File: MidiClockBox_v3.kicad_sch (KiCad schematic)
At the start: 69 parts, among them J1 Midi In 0, J10 Display, J11 Midi Out 3, J12 Midi Out 4, J13 Midi Out 5, J14 Sync Out 0, J15 Sync Out 1, J16 Conn_01x08, J2 ICSP, J3 Conn_02x09_Odd_Even, J4 Conn_02x04_Odd_Even, J5 Conn_02x12_Counter_Clockwise, J6 Midi Out 0, J7 Midi Out 1, J8 Midi Out 2, J9 WS2812, SW1 RotaryEncoder_Switch, U1 CD74HC4067SM, U2 74LS241, U3 6N138, U4 74HC595, U6 74LS08, U7 74LS08, U8 74HC595, U9 74LS241

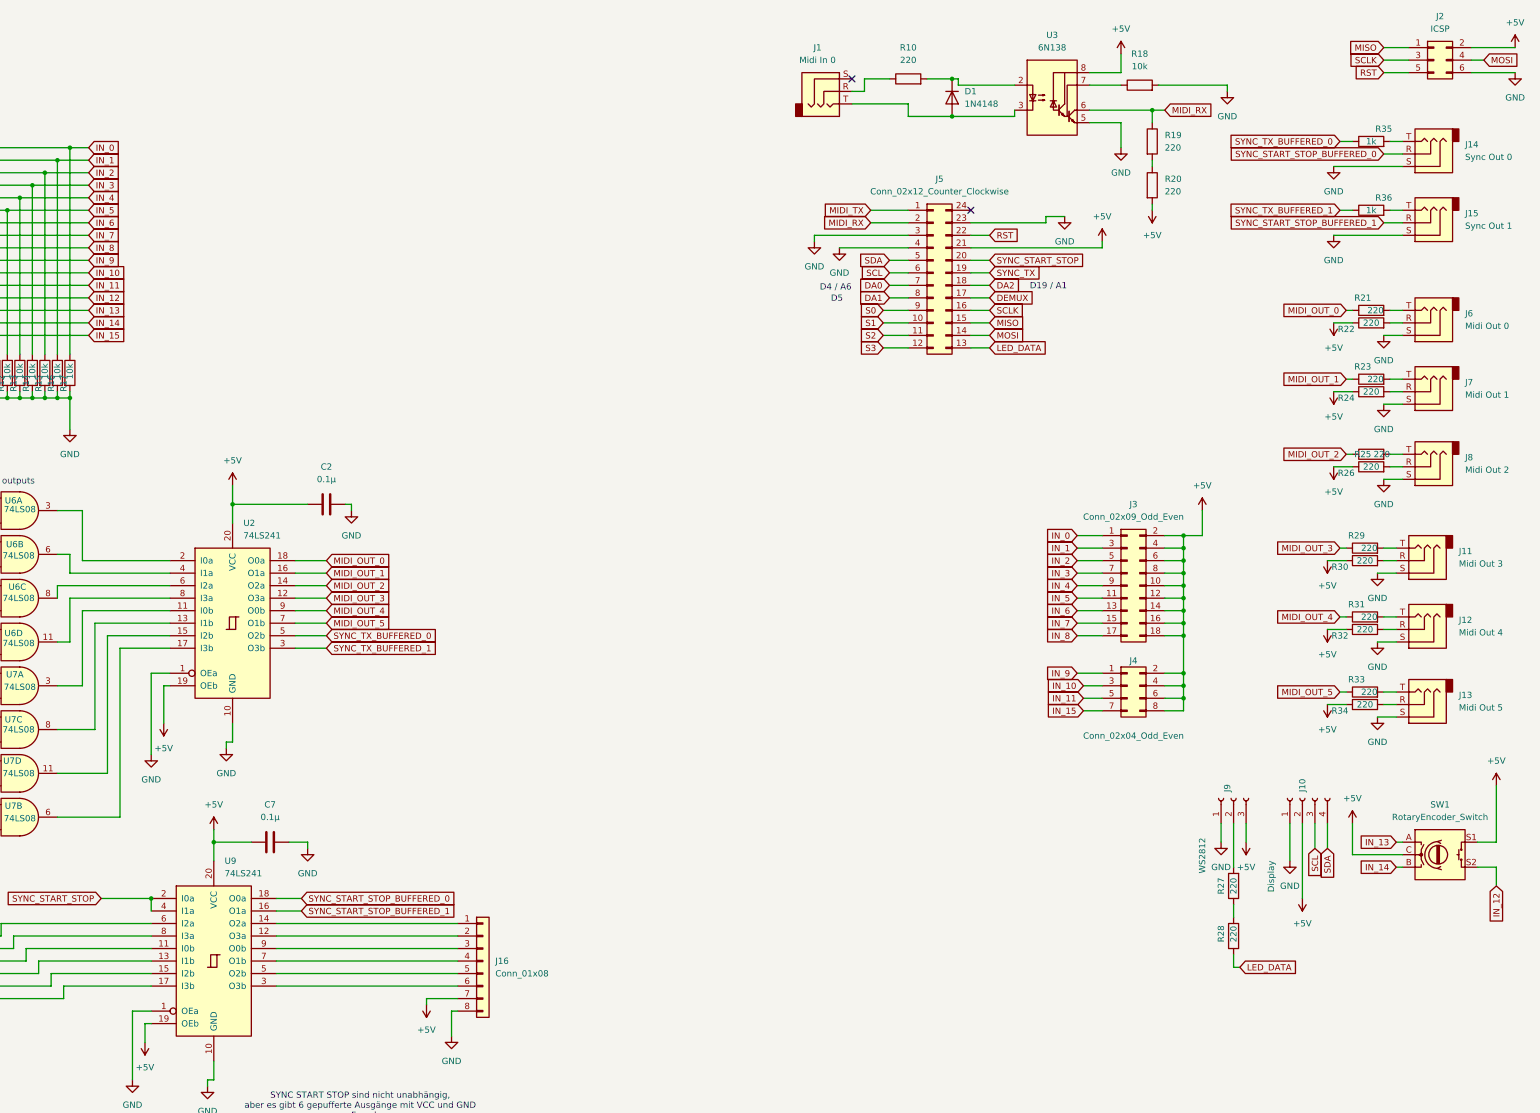
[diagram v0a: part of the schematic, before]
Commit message: add edge cuts
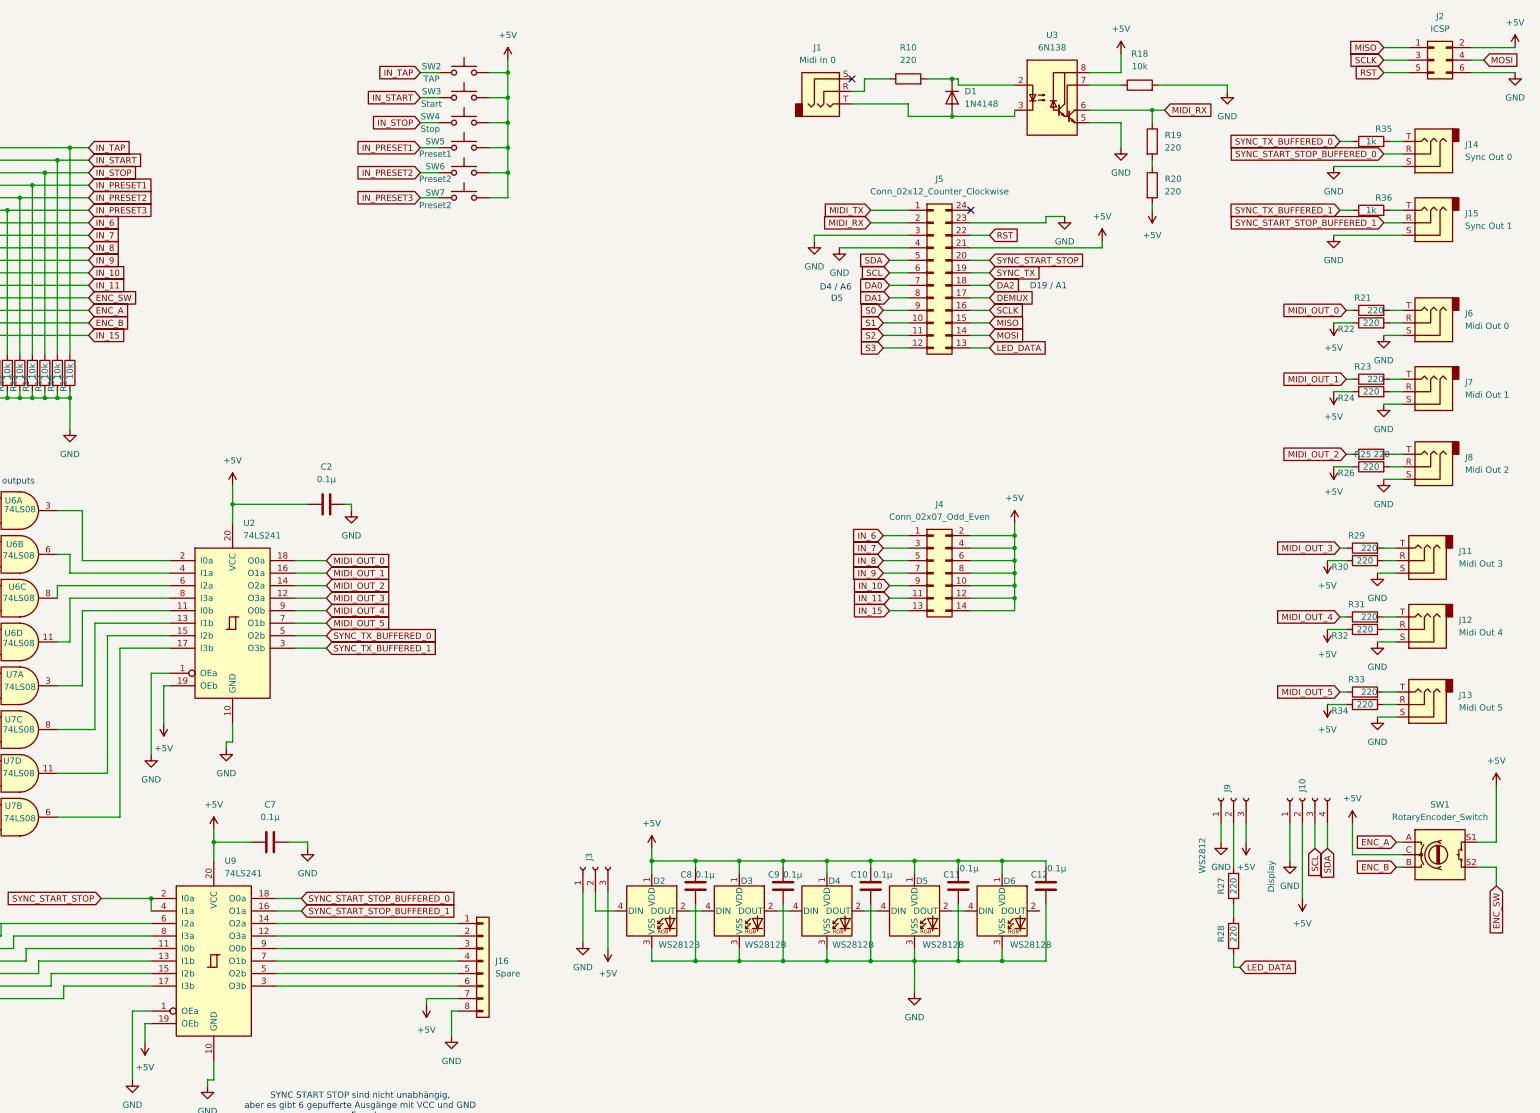
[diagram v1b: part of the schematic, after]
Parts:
- removed J3: Conn_02x09_Odd_Even, Connector_PinHeader_2.54mm:PinHeader_2x09_P2.54mm_Vertical, symbol Connector_Generic:Conn_02x09_Odd_Even
- removed J4: Conn_02x04_Odd_Even, Connector_PinHeader_2.54mm:PinHeader_2x04_P2.54mm_Vertical, symbol Connector_Generic:Conn_02x04_Odd_Even
- added C10, C11, C12, C8, C9: 0.1µ, Capacitor_SMD:C_0603_1608Metric, symbol Device:C
- added D2, D3, D4, D5, D6: WS2812B, LED_SMD:LED_WS2812B_PLCC4_5.0x5.0mm_P3.2mm, symbol LED:WS2812B
- added J3: WS2812, Connector_PinHeader_2.54mm:PinHeader_1x03_P2.54mm_Vertical, symbol Connector:Conn_01x03_Socket
- added J4: Conn_02x07_Odd_Even, Connector_PinHeader_2.54mm:PinHeader_2x07_P2.54mm_Vertical, symbol Connector_Generic:Conn_02x07_Odd_Even
- added SW2: TAP, Button_Switch_THT:SW_PUSH-12mm_Wuerth-430476085716, symbol Switch:SW_Push
- added SW3: Start, Button_Switch_THT:SW_PUSH-12mm_Wuerth-430476085716, symbol Switch:SW_Push
- added SW4: Stop, Button_Switch_THT:SW_PUSH-12mm_Wuerth-430476085716, symbol Switch:SW_Push
- added SW5: Preset1, Button_Switch_THT:SW_PUSH-12mm_Wuerth-430476085716, symbol Switch:SW_Push
- added SW6, SW7: Preset2, Button_Switch_THT:SW_PUSH-12mm_Wuerth-430476085716, symbol Switch:SW_Push
- J16: value Conn_01x08 -> Spare
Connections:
- net +5V: now also C10.1, C11.1, C12.1, C8.1, C9.1, D2.1 (VDD), D3.1 (VDD), D4.1 (VDD), D5.1 (VDD), D6.1 (VDD), J3.3 (Pin_3), J4.10 (Pin_10), J4.12 (Pin_12), J4.14 (Pin_14), J4.2 (Pin_2), J4.4 (Pin_4), J4.6 (Pin_6), J4.8 (Pin_8), SW2.2, SW3.2, SW4.2, SW5.2, SW6.2, SW7.2
- net GND: now also C10.2, C11.2, C12.2, C8.2, C9.2, D2.3 (VSS), D3.3 (VSS), D4.3 (VSS), D5.3 (VSS), D6.3 (VSS), J3.1 (Pin_1)
- net IN_10: now also J4.9 (Pin_9)
- net IN_11: now also J4.11 (Pin_11)
- net IN_15: now also J4.13 (Pin_13)
- net IN_6: now also J4.1 (Pin_1)
- net IN_7: now also J4.3 (Pin_3)
- net IN_8: now also J4.5 (Pin_5)
- net IN_9: now also J4.7 (Pin_7)
- net IN_0 renamed IN_TAP
- net IN_TAP: now also SW2.1
- net IN_1 renamed IN_START
- net IN_START: now also SW3.1
- net IN_12 renamed ENC_SW
- net IN_13 renamed ENC_A
- net IN_14 renamed ENC_B
- net IN_2 renamed IN_STOP
- net IN_STOP: now also SW4.1
- net IN_3 renamed IN_PRESET1
- net IN_PRESET1: now also SW5.1
- net IN_4 renamed IN_PRESET2
- net IN_PRESET2: now also SW6.1
- net IN_5 renamed IN_PRESET3
- net IN_PRESET3: now also SW7.1
- new net: D2.2 (DOUT), D3.4 (DIN)
- new net: D2.4 (DIN), J3.2 (Pin_2)
- new net: D4.2 (DOUT), D5.4 (DIN)
- new net: D3.2 (DOUT), D4.4 (DIN)
- new net: D5.2 (DOUT), D6.4 (DIN)

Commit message: add recent changes
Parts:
- SW7: value Preset2 -> Preset3
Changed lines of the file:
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@@
 			)
 		)
-		(property "Value" "Preset2"
+		(property "Value" "Preset3"
 			(at 183.388 52.324 0)
 			(effects

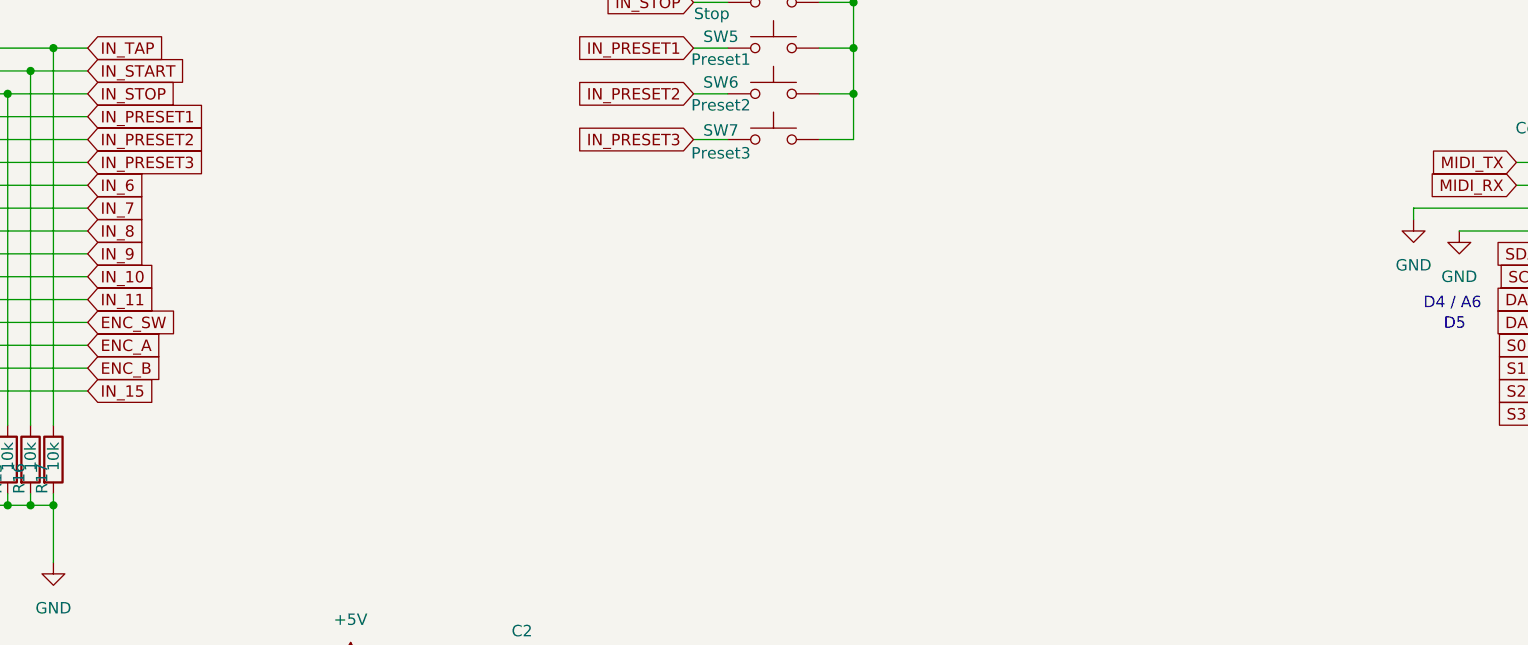
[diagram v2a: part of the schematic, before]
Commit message: add breakout connectors for sync-out and midi-in
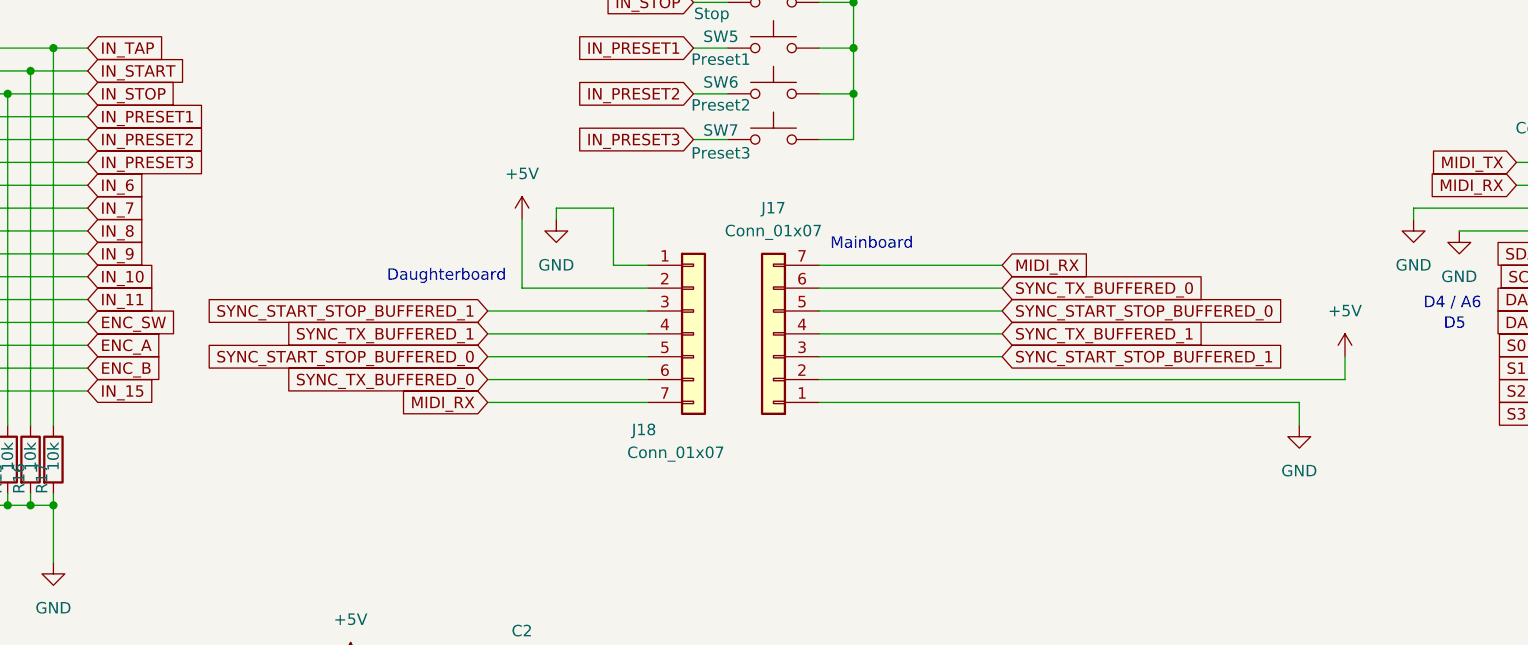
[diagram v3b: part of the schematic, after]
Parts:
- added J17, J18: Conn_01x07, Connector_PinHeader_2.54mm:PinHeader_1x07_P2.54mm_Vertical, symbol Connector_Generic:Conn_01x07
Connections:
- net +5V: now also J17.2 (Pin_2), J18.2 (Pin_2)
- net GND: now also J17.1 (Pin_1), J18.1 (Pin_1)
- net MIDI_RX: now also J17.7 (Pin_7), J18.7 (Pin_7)
- net SYNC_START_STOP_BUFFERED_0: now also J17.5 (Pin_5), J18.5 (Pin_5)
- net SYNC_START_STOP_BUFFERED_1: now also J17.3 (Pin_3), J18.3 (Pin_3)
- net SYNC_TX_BUFFERED_0: now also J17.6 (Pin_6), J18.6 (Pin_6)
- net SYNC_TX_BUFFERED_1: now also J17.4 (Pin_4), J18.4 (Pin_4)
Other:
- note added: "Daughterboard"
- note added: "Mainboard"

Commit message: pcb looks complete
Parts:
- added J19, J20: Conn_02x05_Odd_Even, Connector_PinHeader_2.54mm:PinHeader_2x05_P2.54mm_Vertical, symbol Connector_Generic:Conn_02x05_Odd_Even
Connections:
- net +5V: now also J19.2 (Pin_2), J20.2 (Pin_2)
- net DEMUX: now also J19.3 (Pin_3), J20.3 (Pin_3)
- net GND: now also J19.1 (Pin_1), J20.1 (Pin_1)
- net LED_DATA: now also D2.4 (DIN), J3.2 (Pin_2), J9.2 (Pin_2), J19.10 (Pin_10), J20.10 (Pin_10); no longer J5.13 (Pin_13)
- net S0: now also J19.4 (Pin_4), J20.4 (Pin_4)
- net S1: now also J19.5 (Pin_5), J20.5 (Pin_5)
- net S2: now also J19.6 (Pin_6), J20.6 (Pin_6)
- net S3: now also J19.7 (Pin_7), J20.7 (Pin_7)
- net SCL: now also J19.9 (Pin_9), J20.9 (Pin_9)
- net SDA: now also J19.8 (Pin_8), J20.8 (Pin_8)
- net at R27.2: now also J5.13 (Pin_13); no longer J9.2 (Pin_2)
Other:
- note added: "Buttonboard"
- note added: "Motherboard"
- moved on the sheet: C10, C11, C12, C8, C9, D2, D3, D4, D5, D6, J3, R27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

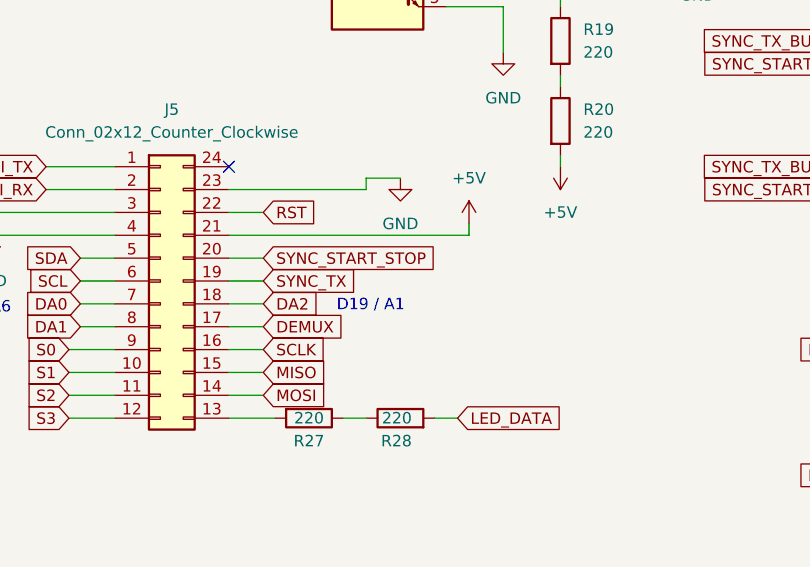
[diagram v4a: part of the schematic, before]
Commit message: change silkscreen info's size
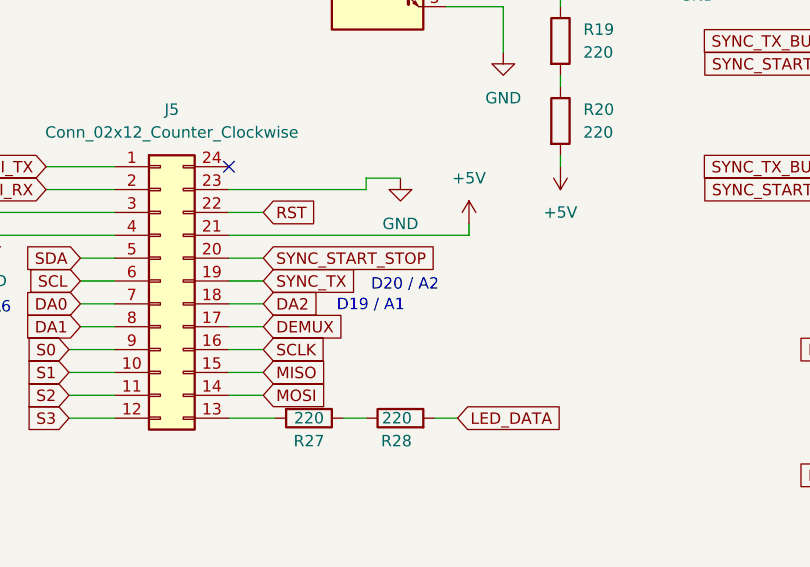
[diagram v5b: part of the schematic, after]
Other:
- note added: "D20 / A2"
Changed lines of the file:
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@@
+		)
+	)
+	(text "D20 / A2"
+		(exclude_from_sim no)
+		(at 311.658 66.548 0)
+		(effects
+			(font
+				(size 1.27 1.27)
+			)
 		)
 	)

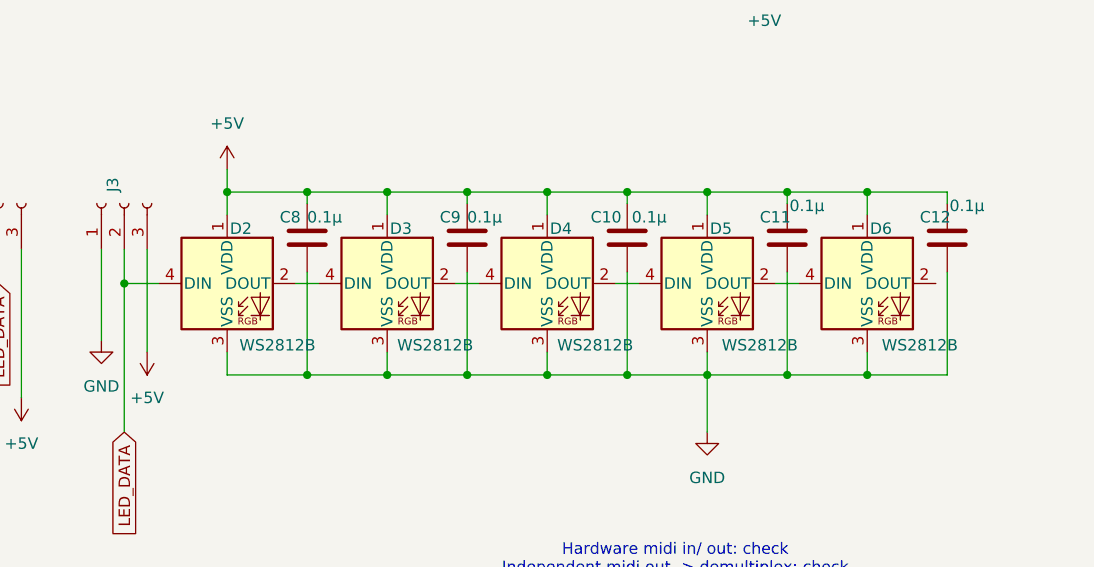
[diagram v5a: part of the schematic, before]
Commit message: fix Adafruit LED pinout and BOM
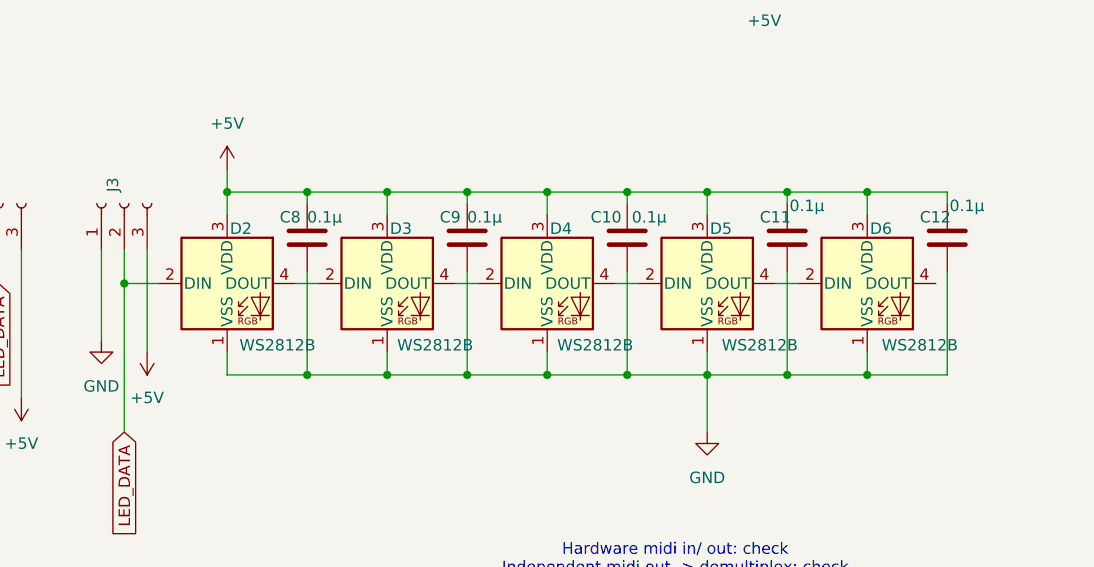
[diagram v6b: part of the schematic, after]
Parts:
- U3: footprint Package_SO:SOP-8_6.62x9.15mm_P2.54mm -> Package_SO:SOP-8_6.605x9.655mm_P2.54mm
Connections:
- net +5V: now also D2.3 (VDD), D3.3 (VDD), D4.3 (VDD), D5.3 (VDD), D6.3 (VDD); no longer D2.1 (VDD), D3.1 (VDD), D4.1 (VDD), D5.1 (VDD), D6.1 (VDD)
- net GND: now also D2.1 (VSS), D3.1 (VSS), D4.1 (VSS), D5.1 (VSS), D6.1 (VSS); no longer D2.3 (VSS), D3.3 (VSS), D4.3 (VSS), D5.3 (VSS), D6.3 (VSS)
- net LED_DATA: now also D2.2 (DIN); no longer D2.4 (DIN)
- net at D3.4 (DOUT): now also D4.2 (DIN); no longer D2.2 (DOUT)
- net at D5.4 (DOUT): now also D6.2 (DIN); no longer D4.2 (DOUT)
- net at D3.2 (DIN): now also D2.4 (DOUT); no longer D4.4 (DIN)
- net at D5.2 (DIN): now also D4.4 (DOUT); no longer D6.4 (DIN)
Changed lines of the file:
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@@
 			)
 		)
-		(property "Footprint" "Package_SO:SOP-8_6.62x9.15mm_P2.54mm"
+		(property "Footprint" "Package_SO:SOP-8_6.605x9.655mm_P2.54mm"
 			(at 315.976 38.1 0)
 			(effects
